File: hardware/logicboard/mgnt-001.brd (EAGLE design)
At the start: 91 x 90 mm, 1 part

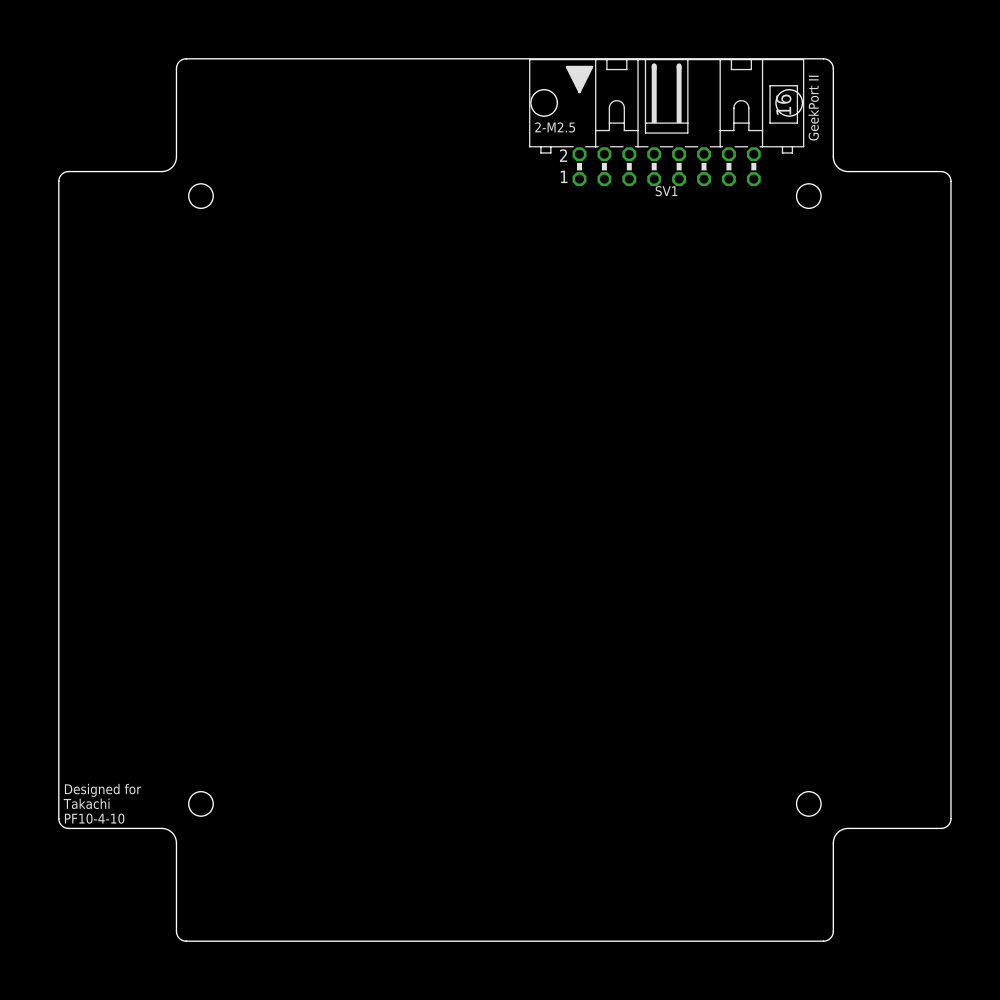
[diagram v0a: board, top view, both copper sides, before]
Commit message: Placed reed sw and other parts.
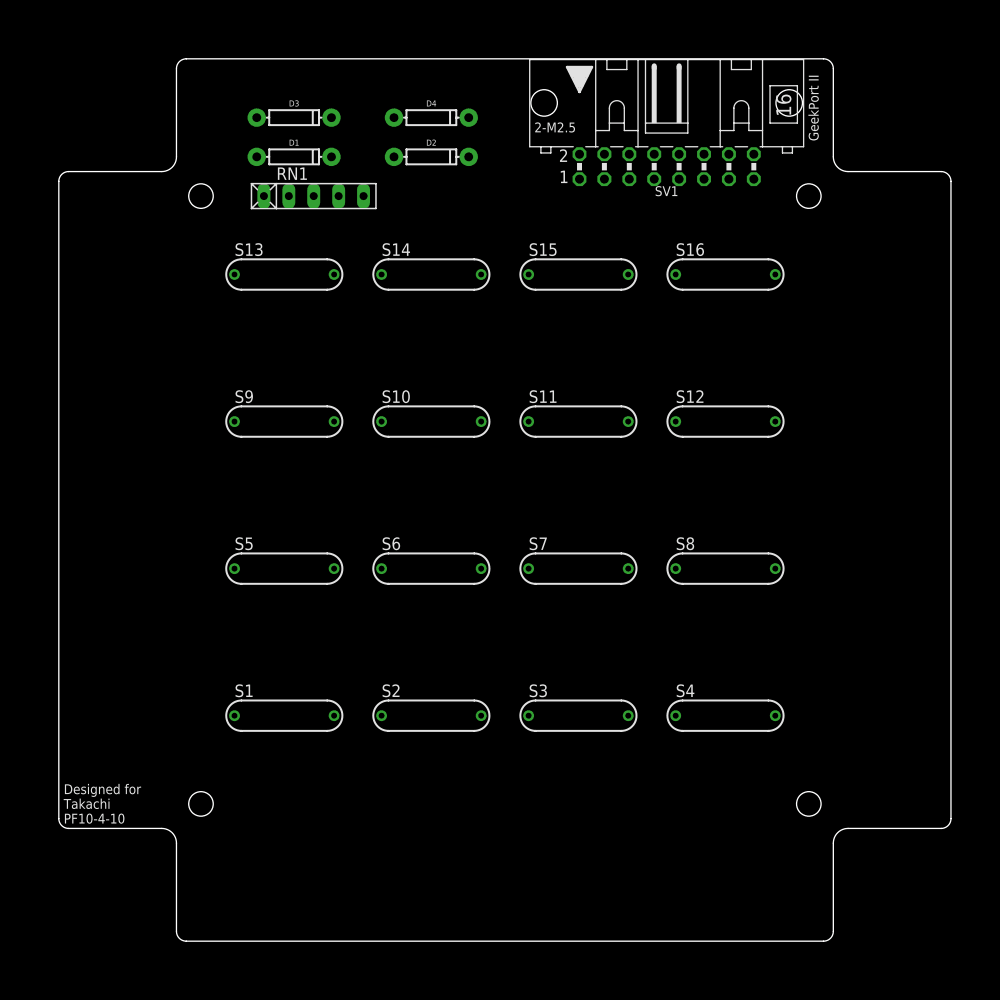
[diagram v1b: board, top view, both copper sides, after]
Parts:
- added D1, D2, D3, D4: 200mA/100V/1V, SparkFun-DiscreteSemi:DIODE-1N4148
- added RN1: (no value), resistor-net:RN-5
- added S1, S10, S11, S12, S13, S14, S15, S16, S2, S3, S4, S5, S6, S7, S8, S9: REED-SWITCH-MK6-4, switch-reed:MK6-4
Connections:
- removed net ANLG0R: SV1.3
- removed net VCC/2: SV1.12, SV1.16, SV1.4, SV1.8
- new net N$1: D1.C, S1.1, S2.1, S3.1, S4.1
- new net N$2: D2.C, S5.1, S6.1, S7.1, S8.1
- new net N$3: D3.C, S10.1, S11.1, S12.1, S9.1
- new net N$4: D4.C, S13.1, S14.1, S15.1, S16.1
- new net N$5: RN1.2, S1.2, S13.2, S5.2, S9.2, SV1.3
- net ANLG1R: now also RN1.3, S10.2, S14.2, S2.2, S6.2
- net ANLG2R: now also RN1.4, S11.2, S15.2, S3.2, S7.2
- net ANLG3R: now also RN1.5, S12.2, S16.2, S4.2, S8.2
- net DTCT0: now also D1.A
- net DTCT1: now also D2.A
- net DTCT2: now also D3.A
- net DTCT3: now also D4.A
- net GND: now also RN1.1

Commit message: First try.
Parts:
- RN1: value (none) -> 103
- moved S1 45.0 mm to (68.0, 23.0), flipped to the bottom
- moved S12 45.0 mm to (23.0, 53.0), flipped to the bottom
- moved S13 45.0 mm to (68.0, 68.0), flipped to the bottom
- moved S16 45.0 mm to (23.0, 68.0), flipped to the bottom
- moved S4 45.0 mm to (23.0, 23.0), flipped to the bottom
- moved S5 45.0 mm to (68.0, 38.0), flipped to the bottom
- moved S8 45.0 mm to (23.0, 38.0), flipped to the bottom
- moved S9 45.0 mm to (68.0, 53.0), flipped to the bottom
- moved D4 41.0 mm to (8.00, 56.0)
- moved D2 34.0 mm to (8.00, 64.0)
- moved SV1 33.0 mm to (29.0, 79.0)
- moved RN1 29.2 mm to (8.00, 53.0)
- moved D3 28.8 mm to (8.00, 60.0)
- moved D1 20.0 mm to (8.00, 68.0)
- moved S10 15.0 mm to (53.0, 53.0), flipped to the bottom
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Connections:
- net N$5 renamed ANLG0R
- removed net N$1: D1.C, S1.1, S2.1, S3.1, S4.1
- removed net N$2: D2.C, S5.1, S6.1, S7.1, S8.1
- removed net N$3: D3.C, S10.1, S11.1, S12.1, S9.1
- removed net N$4: D4.C, S13.1, S14.1, S15.1, S16.1
- net DTCT0: now also D1.C, S1.1, S2.1, S3.1, S4.1
- net DTCT1: now also D2.C, S5.1, S6.1, S7.1, S8.1
- net DTCT2: now also D3.C, S10.1, S11.1, S12.1, S9.1
- net DTCT3: now also D4.C, S13.1, S14.1, S15.1, S16.1
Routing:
- net ANLG0R: track 0.00 -> 140.1 mm
- net DTCT0: track 0.00 -> 126.5 mm
- net DTCT1: track 0.00 -> 110.2 mm, vias 0 -> 1
- net DTCT2: track 0.00 -> 103.6 mm
- net ANLG1R: track 0.00 -> 102.9 mm, vias 0 -> 1
- net DTCT3: track 0.00 -> 89.6 mm
- net ANLG2R: track 0.00 -> 77.8 mm
- net ANLG3R: track 0.00 -> 73.9 mm
- net GND: track 0.00 -> 49.4 mm
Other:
- board text added: "Magnetic 0.0.0-X"
- board text removed: "1"
- board text removed: "2"
- board text removed: "2-BSS138"
- board text removed: "2-M2.5"
- board text removed: "3"
- board text removed: "3.3V I2C"
- board text removed: "4"
- board text removed: "4-103"
- board text removed: "5"
- board text removed: "5V I2C***"
- board text removed: "Bridge here to connect Vcc/2 and GND"
- board text removed: "Bridge to bypass 4066"
- board text removed: "C."
- board text removed: "GPIO"
- board text removed: "I2C/THS*/MNTR"
- board text removed: "IN"
- board text removed: "MIDI"
- board text removed: "MIDI IN"
- board text removed: "MIDI OUT"
- board text removed: "MIDI THRU"
- board text removed: "MKR"
- board text removed: "N.C."
- board text removed: "N.O."
- board text removed: "OUT"
- board text removed: "OUT2"
- board text removed: "PWR"
- board text removed: "RLY"
- board text removed: "Relay-Common"
- board text removed: "Relay-N.C."
- board text removed: "Relay-N.O."
- board text removed: "SPI"
- board text removed: "THS*"
- board text removed: "V+"
- board text removed: "V/2"
- board text removed: "Vcc"
- board text removed: "Vcc/2"
- board text removed: "Vdd"
- board text removed: "Vin"
- board text removed: "Vo"
- board text removed: "Vout"

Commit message: Routed.
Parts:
- added U$1: PINEAPPLELOGO2, pineapplelogo:PINEAPPLELOGO2
- moved D1 60.1 mm to (68.0, 72.0)
- moved RN1 51.3 mm to (45.5, 18.0)
- moved D2 45.7 mm to (53.0, 72.0)
- moved D3 32.3 mm to (38.0, 72.0)
- moved D4 21.9 mm to (23.0, 72.0)
- moved SV1 16.5 mm to (45.5, 79.0)
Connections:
- new net DTCT0D: D1.C, S1.1, S2.1, S3.1, S4.1
- new net DTCT1D: D2.C, S5.1, S6.1, S7.1, S8.1
- new net DTCT2D: D3.C, S10.1, S11.1, S12.1, S9.1
- new net DTCT3D: D4.C, S13.1, S14.1, S15.1, S16.1
- net DTCT0: no longer D1.C, S1.1, S2.1, S3.1, S4.1
- net DTCT1: no longer D2.C, S5.1, S6.1, S7.1, S8.1
- net DTCT2: no longer D3.C, S10.1, S11.1, S12.1, S9.1
- net DTCT3: no longer D4.C, S13.1, S14.1, S15.1, S16.1
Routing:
- net DTCT0D: track 0.00 -> 97.8 mm
- net DTCT0: track 126.5 -> 32.0 mm
- net DTCT1: track 110.2 -> 16.5 mm, vias 1 -> 0
- net DTCT2: track 103.6 -> 18.9 mm
- net DTCT1D: track 0.00 -> 82.2 mm
- net DTCT2D: track 0.00 -> 67.8 mm
- net ANLG3R: track 73.9 -> 130.4 mm
- net DTCT3: track 89.6 -> 37.1 mm
- net DTCT3D: track 0.00 -> 52.2 mm
- net ANLG0R: track 140.1 -> 96.9 mm, vias 0 -> 1
- net ANLG1R: track 102.9 -> 63.2 mm, vias 1 -> 0
- net GND: track 49.4 -> 77.9 mm
- net ANLG2R: track 77.8 -> 82.9 mm
- added copper zone on layer 1, net GND
- added copper zone on layer 16, net GND

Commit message: Routed.
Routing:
- net GND: track 77.9 -> 90.8 mm
- net ANLG3R: track 130.4 -> 125.1 mm
- net DTCT1: track 16.5 -> 11.7 mm
- net DTCT2: track 18.9 -> 21.0 mm
- net DTCT0D: track 97.8 -> 96.2 mm
- net DTCT2D: track 67.8 -> 66.5 mm
- net DTCT1D: track 82.2 -> 81.1 mm
- net ANLG1R: track 63.2 -> 62.3 mm
- net DTCT3D: track 52.2 -> 51.3 mm
- net ANLG2R: track 82.9 -> 83.8 mm
- net ANLG0R: track 96.9 -> 96.3 mm
